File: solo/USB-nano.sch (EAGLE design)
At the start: 19 parts, among them U1 USB_TRACES_NANO

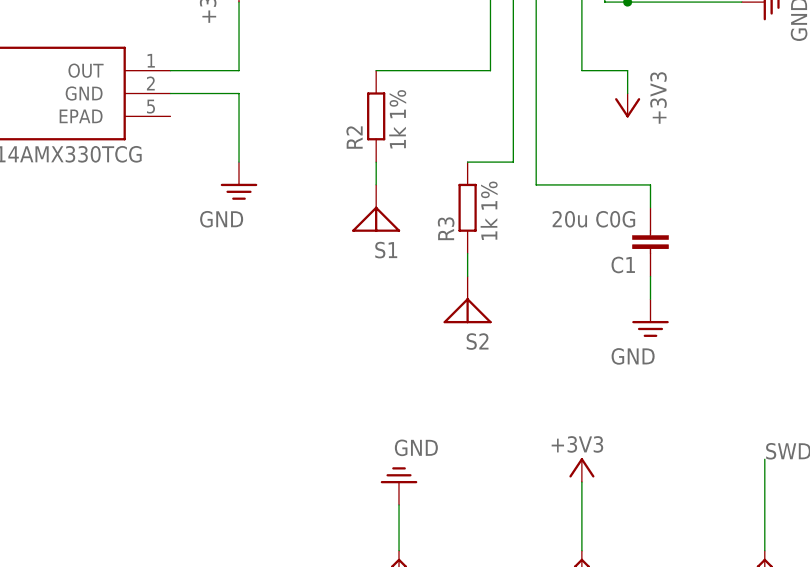
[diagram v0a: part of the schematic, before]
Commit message: update button outline
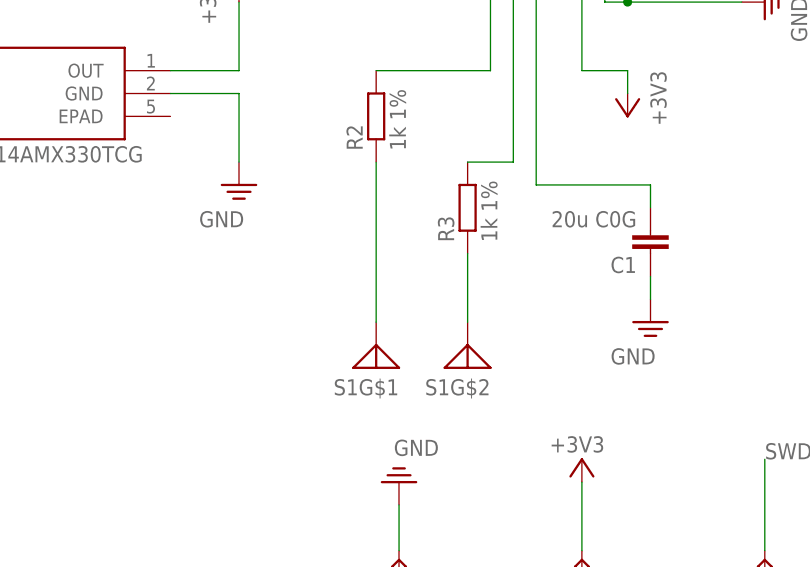
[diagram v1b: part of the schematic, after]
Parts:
- removed S2: TOUCH_SENSOR, efm-fido:TOUCH_SENSOR
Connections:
- net N$2: now also S1G$1.1; no longer S1.1
- net N$5: now also S1G$2.1; no longer S2.1
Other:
- moved on the sheet: S1G$1
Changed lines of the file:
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@@
 <?xml version="1.0" encoding="utf-8"?>
 <!DOCTYPE eagle SYSTEM "eagle.dtd">
-<eagle version="9.3.0">
+<eagle version="9.3.2">
 <drawing>
 <settings>
@@
 <part name="U1" library="efm-fido" library_urn="urn:adsk.eagle:library:4245354" deviceset="USB_TRACES_NANO" device="" package3d_urn="urn:adsk.eagle:package:10400516/6"/>
 <part name="SUPPLY4" library="supply2" library_urn="urn:adsk.eagle:library:372" deviceset="PE" device="" value="GND"/>
-<part name="S1" library="efm-fido" library_urn="urn:adsk.eagle:library:4245354" deviceset="TOUCH_SENSOR" device="" package3d_urn="urn:adsk.eagle:package:10401338/2"/>
 <part name="R2" library="efm-fido" library_urn="urn:adsk.eagle:library:4245354" deviceset="RESISTOR" device="" package3d_urn="urn:adsk.eagle:package:4245807/8" value="1k 1%"/>
 <part name="C1" library="efm-fido" library_urn="urn:adsk.eagle:library:4245354" deviceset="CAPACITOR" device="" package3d_urn="urn:adsk.eagle:package:4245806/9" value="20u C0G"/>
 <part name="SUPPLY1" library="supply2" library_urn="urn:adsk.eagle:library:372" deviceset="PE" device="" value="GND"/>
-<part name="S2" library="efm-fido" library_urn="urn:adsk.eagle:library:4245354" deviceset="TOUCH_SENSOR" device="" package3d_urn="urn:adsk.eagle:package:10401338/2"/>
 <part name="R3" library="efm-fido" library_urn="urn:adsk.eagle:library:4245354" deviceset="RESISTOR" device="" package3d_urn="urn:adsk.eagle:package:4245807/8" value="1k 1%"/>
+<part name="S1" library="efm-fido" library_urn="urn:adsk.eagle:library:4245354" deviceset="TOUCH_SENSOR" device="" package3d_urn="urn:adsk.eagle:package:10401338/5"/>
 </parts>
 <sheets>
@@
 <attribute name="VALUE" x="85.725" y="139.319" size="1.778" layer="96" rot="R180"/>
 </instance>
-<instance part="S1" gate="G$1" x="154.94" y="45.72" smashed="yes" rot="R180">
-<attribute name="NAME" x="157.48" y="44.45" size="1.778" layer="95" rot="R180"/>
-</instance>
 <instance part="R2" gate="G$1" x="154.94" y="58.42" smashed="yes" rot="R90">
 <attribute name="NAME" x="153.4414" y="54.61" size="1.778" layer="95" rot="R90"/>
@@
 <attribute name="VALUE" x="180.975" y="30.861" size="1.778" layer="96"/>
 </instance>
-<instance part="S2" gate="G$1" x="165.1" y="35.56" smashed="yes" rot="R180">
-<attribute name="NAME" x="167.64" y="34.29" size="1.778" layer="95" rot="R180"/>
-</instance>
 <instance part="R3" gate="G$1" x="165.1" y="48.26" smashed="yes" rot="R90">
 <attribute name="NAME" x="163.6014" y="44.45" size="1.778" layer="95" rot="R90"/>
 <attribute name="VALUE" x="168.402" y="44.45" size="1.778" layer="96" rot="R90"/>
+</instance>
+<instance part="S1" gate="G$1" x="154.94" y="30.48" smashed="yes" rot="R180">
+<attribute name="NAME" x="157.48" y="29.21" size="1.778" layer="95" rot="R180"/>
+</instance>
+<instance part="S1" gate="G$2" x="165.1" y="30.48" smashed="yes" rot="R180">
+<attribute name="NAME" x="167.64" y="29.21" size="1.778" layer="95" rot="R180"/>
 </instance>
 </instances>
@@
 <net name="N$2" class="0">
 <segment>
+<pinref part="R2" gate="G$1" pin="1"/>
+<wire x1="154.94" y1="35.56" x2="154.94" y2="53.34" width="0.1524" layer="91"/>
 <pinref part="S1" gate="G$1" pin="1"/>
-<pinref part="R2" gate="G$1" pin="1"/>
-<wire x1="154.94" y1="50.8" x2="154.94" y2="53.34" width="0.1524" layer="91"/>
 </segment>
 </net>
@@
 <net name="N$5" class="0">
 <segment>
-<pinref part="S2" gate="G$1" pin="1"/>
 <pinref part="R3" gate="G$1" pin="1"/>
-<wire x1="165.1" y1="40.64" x2="165.1" y2="43.18" width="0.1524" layer="91"/>
-</segment>
-</net>
+<wire x1="165.1" y1="35.56" x2="165.1" y2="43.18" width="0.1524" layer="91"/>
+<pinref part="S1" gate="G$2" pin="1"/>
+</segment>
+</net>
